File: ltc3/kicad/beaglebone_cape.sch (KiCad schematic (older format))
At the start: 8 parts, among them U301 24C256

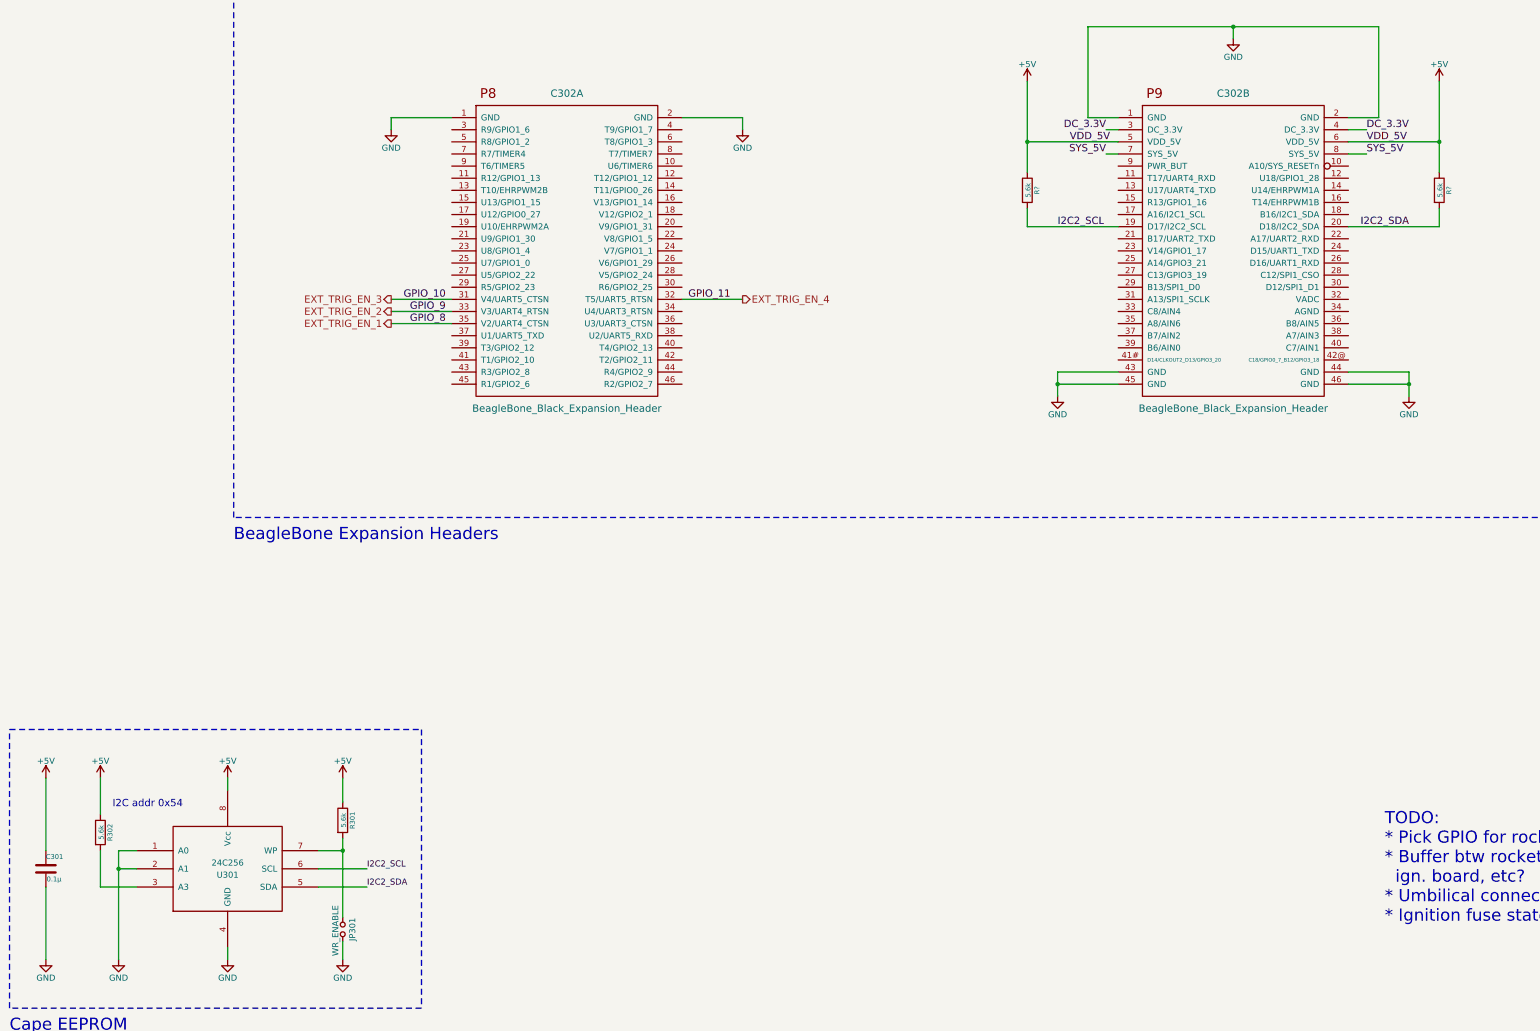
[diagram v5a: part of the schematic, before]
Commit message: LTC3: Reordered schematic sub-sheets; updated PDF export of schematic.
KiCad has an odd habit of ordering a schematic's sub-sheets without
notice.
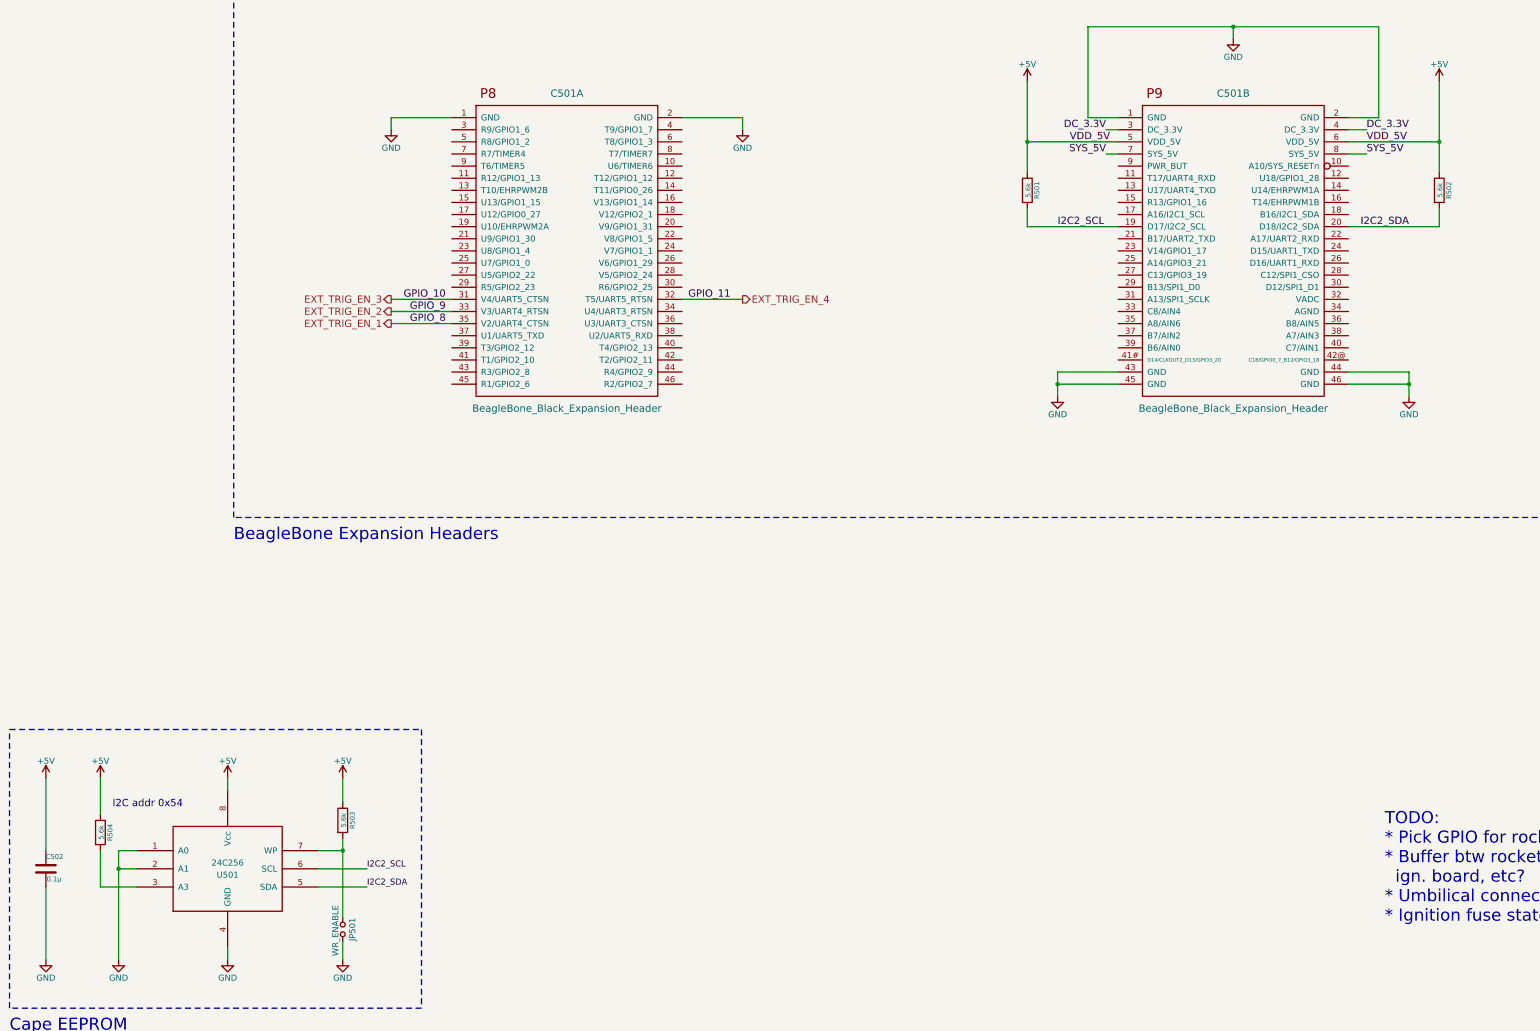
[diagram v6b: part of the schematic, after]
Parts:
- gave numbers to parts that had none: 2
- renumbered C302 to C501, C301 to C502, JP301 to JP501, R301 to R503, R302 to R504, U301 to U501
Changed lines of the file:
@@
 Sheet 3 7
 Title "LTC3 BeagleBone Black Cape Interface"
-Date "2015-11-20"
+Date "2015-11-25"
 Rev "A"
 Comp "Portland State Aerospace Society <http://psas.pdx.edu/>"
@@
 I2C2_SDA
 $Comp
-L C C301
+L C C502
 U 1 1 55052668
 P 1250 8700
-F 0 "C301" H 1250 8800 40  0000 L CNN
+F 0 "C502" H 1250 8800 40  0000 L CNN
 F 1 "0.1μ" H 1256 8615 40  0000 L CNN
 F 2 "~" H 1288 8550 30  0000 C CNN
@@
 $EndComp
 $Comp
-L R R302
+L R R504
 U 1 1 55052963
 P 1700 8400
-F 0 "R302" V 1780 8400 40  0000 C CNN
+F 0 "R504" V 1780 8400 40  0000 C CNN
 F 1 "5.6k" V 1707 8401 40  0000 C CNN
 F 2 "~" V 1630 8400 30  0000 C CNN
@@
 $EndComp
 $Comp
-L R R301
+L R R503
 U 1 1 55052990
 P 3700 8300
-F 0 "R301" V 3780 8300 40  0000 C CNN
+F 0 "R503" V 3780 8300 40  0000 C CNN
 F 1 "5.6k" V 3707 8301 40  0000 C CNN
 F 2 "~" V 3630 8300 30  0000 C CNN
@@
 TODO: connect these labels\nto BBB GPIO pins.
 $Comp
-L GND #PWR312
+L GND #PWR514
 U 1 1 557C941A
 P 2750 9450
-F 0 "#PWR312" H 2750 9200 50  0001 C CNN
+F 0 "#PWR514" H 2750 9200 50  0001 C CNN
 F 1 "GND" H 2750 9300 50  0000 C CNN
 F 2 "" H 2750 9450 60  0000 C CNN
@@
 $EndComp
 $Comp
-L Jumper_NO_Small JP301
+L Jumper_NO_Small JP501
 U 1 1 557CBDCC
 P 3700 9200
-F 0 "JP301" H 3700 9280 50  0000 C CNN
+F 0 "JP501" H 3700 9280 50  0000 C CNN
 F 1 "WR_ENABLE" H 3710 9140 50  0000 C CNN
 F 2 "" H 3700 9200 60  0000 C CNN
@@
 $EndComp
 $Comp
-L GND #PWR313
+L GND #PWR515
 U 1 1 557CCCE2
 P 3700 9450
-F 0 "#PWR313" H 3700 9200 50  0001 C CNN
+F 0 "#PWR515" H 3700 9200 50  0001 C CNN
 F 1 "GND" H 3700 9300 50  0000 C CNN
 F 2 "" H 3700 9450 60  0000 C CNN
@@
 $EndComp
 $Comp
-L GND #PWR311
+L GND #PWR513
 U 1 1 557CCE7C
 P 1850 9450
-F 0 "#PWR311" H 1850 9200 50  0001 C CNN
+F 0 "#PWR513" H 1850 9200 50  0001 C CNN
 F 1 "GND" H 1850 9300 50  0000 C CNN
 F 2 "" H 1850 9450 60  0000 C CNN
@@
 $EndComp
 $Comp
-L GND #PWR310
+L GND #PWR512
 U 1 1 557CE60A
 P 1250 9450
-F 0 "#PWR310" H 1250 9200 50  0001 C CNN
+F 0 "#PWR512" H 1250 9200 50  0001 C CNN
 F 1 "GND" H 1250 9300 50  0000 C CNN
 F 2 "" H 1250 9450 60  0000 C CNN
@@
 	4100 4100 4600 4100
 $Comp
-L BeagleBone_Black_Expansion_Header C302
+L BeagleBone_Black_Expansion_Header C501
 U 1 1 55E6D53E
 P 5550 3500
-F 0 "C302" H 5550 4700 60  0000 C CNN
+F 0 "C501" H 5550 4700 60  0000 C CNN
 F 1 "BeagleBone_Black_Expansion_Header" H 5550 2100 60  0000 C CNN
 F 2 "" H 5550 3500 60  0000 C CNN
@@
 $EndComp
 $Comp
-L BeagleBone_Black_Expansion_Header C302
+L BeagleBone_Black_Expansion_Header C501
 U 2 1 55E6D67B
 P 11050 3500
-F 0 "C302" H 11050 4700 60  0000 C CNN
+F 0 "C501" H 11050 4700 60  0000 C CNN
 F 1 "BeagleBone_Black_Expansion_Header" H 11050 2100 60  0000 C CNN
 F 2 "" H 11050 3500 60  0000 C CNN
@@
 	4600 4000 4100 4000
 $Comp
-L GND #PWR308
+L GND #PWR504
 U 1 1 55E75ADE
 P 4100 2600
-F 0 "#PWR308" H 4100 2350 50  0001 C CNN
+F 0 "#PWR504" H 4100 2350 50  0001 C CNN
 F 1 "GND" H 4100 2450 50  0000 C CNN
 F 2 "" H 4100 2600 60  0000 C CNN
@@
 	4100 2500 4600 2500
 $Comp
-L GND #PWR309
+L GND #PWR505
 U 1 1 55E75BB5
 P 7000 2600
-F 0 "#PWR309" H 7000 2350 50  0001 C CNN
+F 0 "#PWR505" H 7000 2350 50  0001 C CNN
 F 1 "GND" H 7000 2450 50  0000 C CNN
 F 2 "" H 7000 2600 60  0000 C CNN
@@
 	7000 2500 6500 2500
 $Comp
-L GND #PWR314
+L GND #PWR506
 U 1 1 55E77963
 P 9600 4800
-F 0 "#PWR314" H 9600 4550 50  0001 C CNN
+F 0 "#PWR506" H 9600 4550 50  0001 C CNN
 F 1 "GND" H 9600 4650 50  0000 C CNN
 F 2 "" H 9600 4800 60  0000 C CNN
@@
 Connection ~ 9600 4700
 $Comp
-L GND #PWR315
+L GND #PWR507
 U 1 1 55E77AD2
 P 12500 4800
-F 0 "#PWR315" H 12500 4550 50  0001 C CNN
+F 0 "#PWR507" H 12500 4550 50  0001 C CNN
 F 1 "GND" H 12500 4650 50  0000 C CNN
 F 2 "" H 12500 4800 60  0000 C CNN
@@
 	10000 2600 10100 2600
 $Comp
-L GND #PWR301
+L GND #PWR501
 U 1 1 55E7923E
 P 11050 1850
-F 0 "#PWR301" H 11050 1600 50  0001 C CNN
+F 0 "#PWR501" H 11050 1600 50  0001 C CNN
 F 1 "GND" H 11050 1700 50  0000 C CNN
 F 2 "" H 11050 1850 60  0000 C CNN
@@
 	12150 2800 12000 2800
 $Comp
-L 24C256 U301
+L 24C256 U501
 U 1 1 560CBFF6
 P 2750 8700
-F 0 "U301" H 2750 8650 50  0000 C CNN
+F 0 "U501" H 2750 8650 50  0000 C CNN
 F 1 "24C256" H 2750 8750 50  0000 C CNN
 F 2 "" H 2750 9000 50  0001 C CNN
@@
 ROCKET_READY
 $Comp
-L +5V #PWR307
+L +5V #PWR503
 U 1 1 565530F5
 P 12750 2200
-F 0 "#PWR307" H 12750 2050 50  0001 C CNN
+F 0 "#PWR503" H 12750 2050 50  0001 C CNN
 F 1 "+5V" H 12750 2340 50  0000 C CNN
 F 2 "" H 12750 2200 60  0000 C CNN
@@
 	12750 2700 12750 2950
 $Comp
-L +5V #PWR306
+L +5V #PWR502
 U 1 1 565538D1
 P 9350 2200
-F 0 "#PWR306" H 9350 2050 50  0001 C CNN
+F 0 "#PWR502" H 9350 2050 50  0001 C CNN
 F 1 "+5V" H 9350 2340 50  0000 C CNN
 F 2 "" H 9350 2200 60  0000 C CNN
@@
 	9350 2700 9350 2950
 $Comp
-L +5V #PWR302
+L +5V #PWR508
 U 1 1 56555506
 P 1250 7950
-F 0 "#PWR302" H 1250 7800 50  0001 C CNN
+F 0 "#PWR508" H 1250 7800 50  0001 C CNN
 F 1 "+5V" H 1250 8090 50  0000 C CNN
 F 2 "" H 1250 7950 60  0000 C CNN
@@
 $EndComp
 $Comp
-L +5V #PWR303
+L +5V #PWR509
 U 1 1 56555577
 P 1700 7950
-F 0 "#PWR303" H 1700 7800 50  0001 C CNN
+F 0 "#PWR509" H 1700 7800 50  0001 C CNN
 F 1 "+5V" H 1700 8090 50  0000 C CNN
 F 2 "" H 1700 7950 60  0000 C CNN
@@
 $EndComp
 $Comp
-L +5V #PWR304
+L +5V #PWR510
 U 1 1 565555AF
 P 2750 7950
-F 0 "#PWR304" H 2750 7800 50  0001 C CNN
+F 0 "#PWR510" H 2750 7800 50  0001 C CNN
 F 1 "+5V" H 2750 8090 50  0000 C CNN
 F 2 "" H 2750 7950 60  0000 C CNN
@@
 $EndComp
 $Comp
-L +5V #PWR305
+L +5V #PWR511
 U 1 1 565555E7
 P 3700 7950
-F 0 "#PWR305" H 3700 7800 50  0001 C CNN
+F 0 "#PWR511" H 3700 7800 50  0001 C CNN
 F 1 "+5V" H 3700 8090 50  0000 C CNN
 F 2 "" H 3700 7950 60  0000 C CNN
@@
 I2C addr 0x54
 $Comp
-L R R?
+L R R502
 U 1 1 5658AA1A
 P 12750 3100
-F 0 "R?" V 12830 3100 40  0000 C CNN
+F 0 "R502" V 12830 3100 40  0000 C CNN
 F 1 "5.6k" V 12757 3101 40  0000 C CNN
 F 2 "~" V 12680 3100 30  0000 C CNN
@@
 $EndComp
 $Comp
-L R R?
+L R R501
 U 1 1 5658AFE1
 P 9350 3100
-F 0 "R?" V 9430 3100 40  0000 C CNN
+F 0 "R501" V 9430 3100 40  0000 C CNN
 F 1 "5.6k" V 9357 3101 40  0000 C CNN
 F 2 "~" V 9280 3100 30  0000 C CNN
